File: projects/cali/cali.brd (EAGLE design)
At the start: 89.8 x 61.9 mm, 28 parts, among them T1 IRLML2502, T2 IRLML2502, T3 2N7002E, T4 IRLML2502

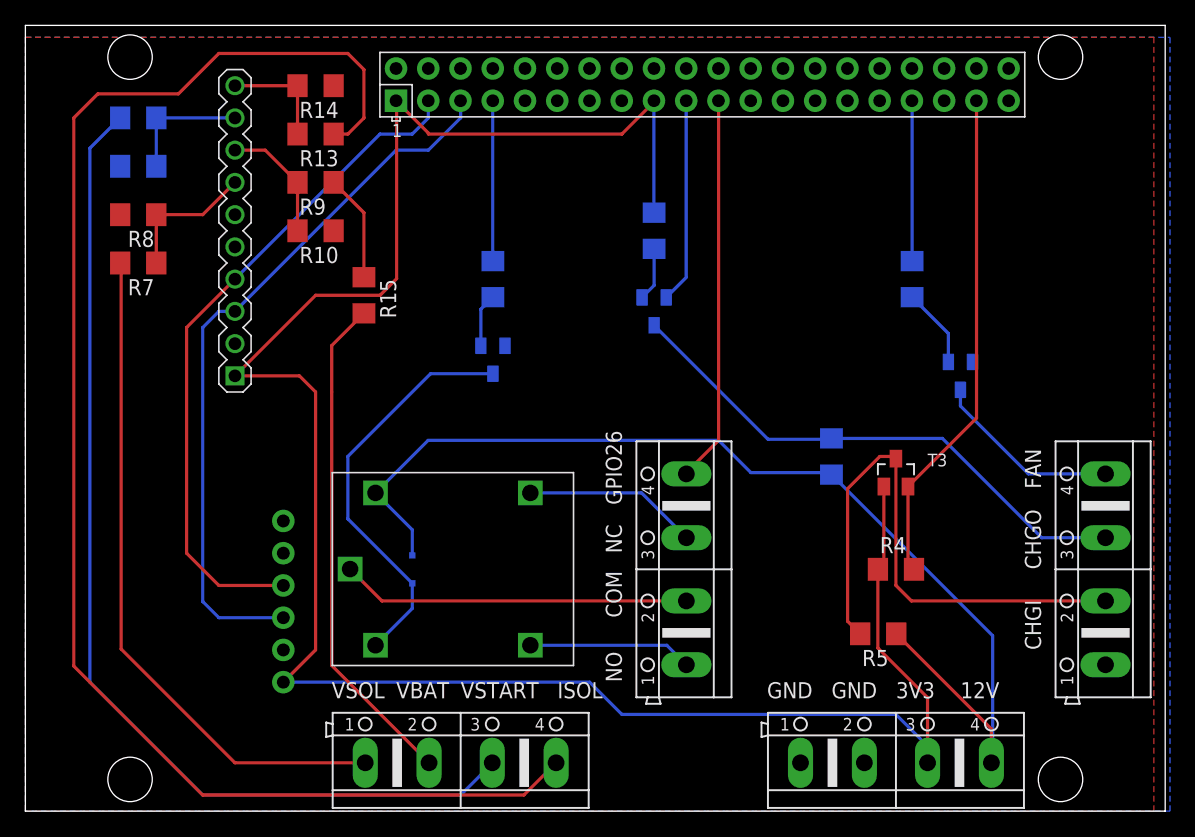
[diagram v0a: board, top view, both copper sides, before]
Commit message: Caliboard 1.2
- Fan output now has a PP stage
- Temp-sensor 4k7 pull up
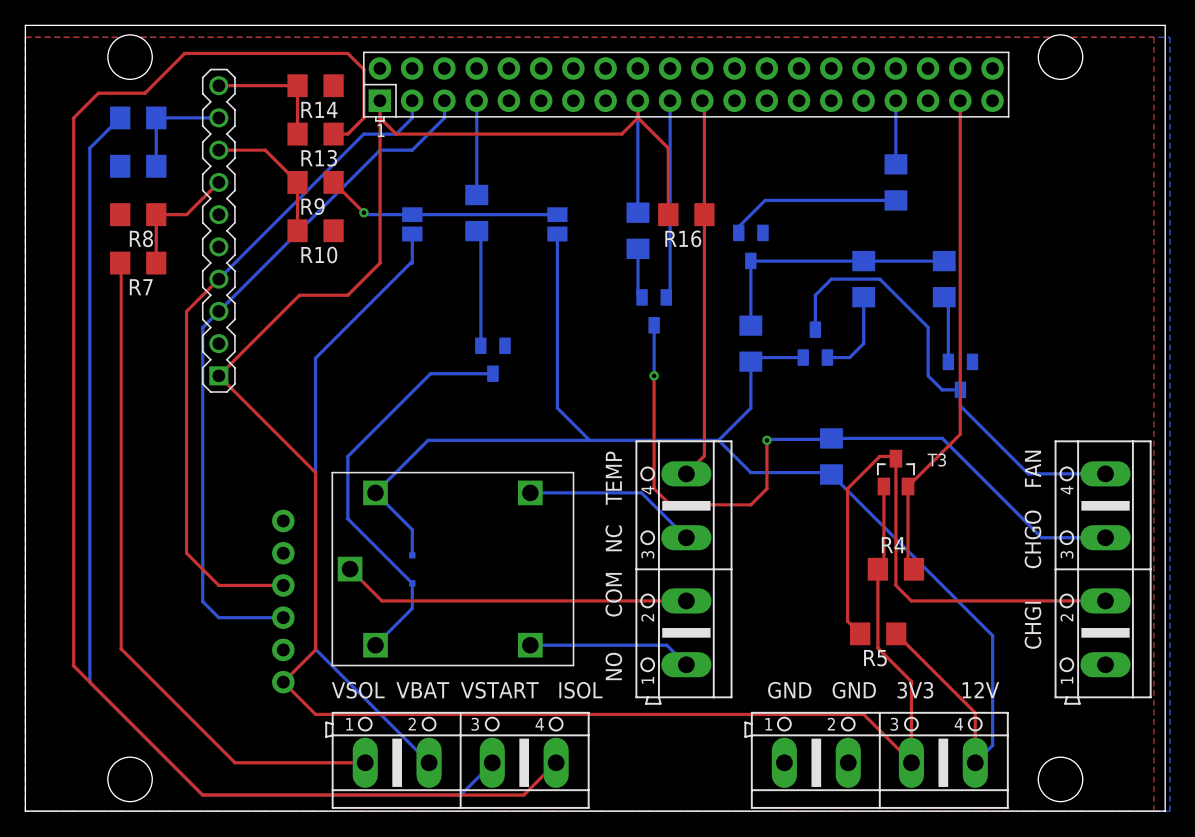
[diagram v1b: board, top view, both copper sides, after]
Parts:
- added R16: 4k7, rcl:R1206
- added R17: 10k, rcl:R1206
- added R18: 100, rcl:R1206
- added SJ1, SJ2: (no value), jumper:SJ
- added T5: IRLML6402, we-transistor:SOT23
- added T6: IRLML2502, we-transistor:SOT23
- R15: value 0 -> 100
- moved R15 39.4 mm to (66.0, 41.9), flipped to the bottom
- moved R6 5.36 mm to (35.6, 47.1)
- moved R1 2.54 mm to (72.4, 41.9)
- moved R2 1.27 mm to (48.3, 45.7)
- moved U$1 1.27 mm to (8.89, 45.7)
- moved U$2 1.27 mm to (19.6, 30.7)
- moved X2 1.27 mm to (67.3, 3.81)
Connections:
- removed net N$9: R15.2, X3.2
- new net /GPIO13: R1.1, R15.1, R17.1, T6.3
- new net N$12: R18.2, T6.1
- new net N$8: R15.2, T5.1
- new net V_BAT: SJ1.1, X3.2
- net +12V: now also R17.2, SJ2.2, T5.2
- net +3V3: now also R16.2
- net GND: now also T6.2
- net GPIO13: now also R18.1; no longer R1.1
- net GPIO9: now also R16.1
- net N$13: now also SJ1.2, SJ2.1; no longer R15.1
- net N$2: now also T5.3
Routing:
- net V_BAT: track 0.00 -> 48.6 mm
- net N$9: track 39.6 -> 0.00 mm
- net +12V: track 86.1 -> 115.0 mm
- net N$2: track 14.9 -> 35.4 mm
- net /GPIO13: track 0.00 -> 20.3 mm
- net N$11: track 42.6 -> 56.8 mm, vias 0 -> 2
- net N$12: track 0.00 -> 13.7 mm
- net N$13: track 8.46 -> 18.8 mm, vias 0 -> 1
- net GPIO13: track 12.6 -> 5.02 mm
- net N$8: track 0.00 -> 6.97 mm
- net GPIO4: track 12.6 -> 7.45 mm
- net N$4: track 4.22 -> 9.17 mm
- net +3V3: track 169.8 -> 172.9 mm
- net SCL: track 57.0 -> 55.7 mm
- net ADC3: track 8.74 -> 10.0 mm
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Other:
- board text added: "(c) Christian Eisendle"
- board text added: "Caliboard 1.2"
- board text added: "TEMP"
- board text removed: "Caliboard 1.1 (c) Christian Eisendle"
- board text removed: "GPIO26"

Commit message: Caliboard 1.4
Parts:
- removed D1: BAS316, nxp_60:SOD323(F)
- removed R15, R18, R2, R6: 100, rcl:R1206
- removed R17, R3, R5: 10k, rcl:R1206
- removed T1, T2, T4, T6: IRLML2502, we-transistor:SOT23
- removed T3: 2N7002E, nxp_60:SOT23
- removed T5: IRLML6402, we-transistor:SOT23
- added D2: BZX384-3V3, nxp_60:SOD323(F)
- added IC1: L293DD, st-microelectronics:SO20
- R1: value 100 -> DNP
- R4: value 1k -> 10k
- moved SJ2 27.6 mm to (37.0, 19.1), turned to 180 degrees
- moved SJ1 27.2 mm to (31.0, 19.1), turned to 180 degrees
- moved R1 26.7 mm to (73.7, 15.2), flipped to the top
- moved R4 24.7 mm to (73.7, 43.2), turned to 270 degrees
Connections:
- removed net /GPIO13: R1.1, R15.1, R17.1, T6.3
- removed net CHGI: R5.1, T3.3, X1.2
- removed net GPIO4: R6.1, U$2.7
- removed net N$1: D1.2, T4.3, U$4.A2
- removed net N$10: R2.1, T2.1
- removed net N$11: R3.1, T2.3, X1.3
- removed net N$12: R18.2, T6.1
- removed net N$4: R6.2, T4.1
- removed net N$8: R15.2, T5.1
- new net DRVOUT3: IC1.13, U$4.A1
- new net GPIO5: IC1.9, U$2.29
- new net GPIO6: IC1.12, U$2.31
- new net N$9: R1.1, R4.2, X1.2
- net +12V: now also IC1.10, IC1.20; no longer D1.1, R17.2, R3.2, R5.2, T5.2, U$4.A1
- net +3V3: now also IC1.1, IC1.11; no longer R2.2, R4.1, T3.1
- net GND: now also D2.2, IC1.14, IC1.15, IC1.16, IC1.17, IC1.19, IC1.4, IC1.5, IC1.6, IC1.7, R1.2, U$4.A2; no longer T1.2, T4.2, T6.2
- net GPIO10: no longer T2.2
- net GPIO13: now also IC1.2; no longer R18.1
- net GPIO26: now also D2.1, R4.1; no longer R4.2, T3.2
- net N$2: now also IC1.3; no longer T1.3, T5.3
- net N$6: now also IC1.8, X1.3; no longer R1.2, T1.1
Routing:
- net N$11: track 56.8 -> 0.00 mm, vias 2 -> 0
- net DRVOUT3: track 0.00 -> 53.5 mm
- net CHGI: track 43.8 -> 0.00 mm
- net N$9: track 0.00 -> 36.6 mm
- net GPIO13: track 5.02 -> 39.8 mm, vias 0 -> 2
- net V_BAT: track 48.6 -> 15.9 mm
- net N$1: track 32.3 -> 0.00 mm
- net GPIO26: track 38.8 -> 11.7 mm
- net +12V: track 115.0 -> 139.6 mm
- net GPIO5: track 0.00 -> 22.4 mm, vias 0 -> 1
- net N$13: track 18.8 -> 39.9 mm
- net /GPIO13: track 20.3 -> 0.00 mm
- net N$2: track 35.4 -> 15.4 mm
- net N$6: track 5.23 -> 23.1 mm
- net GPIO10: track 15.6 -> 0.00 mm
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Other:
- board text added: "Caliboard 1.4"
- board text removed: "Caliboard 1.2"

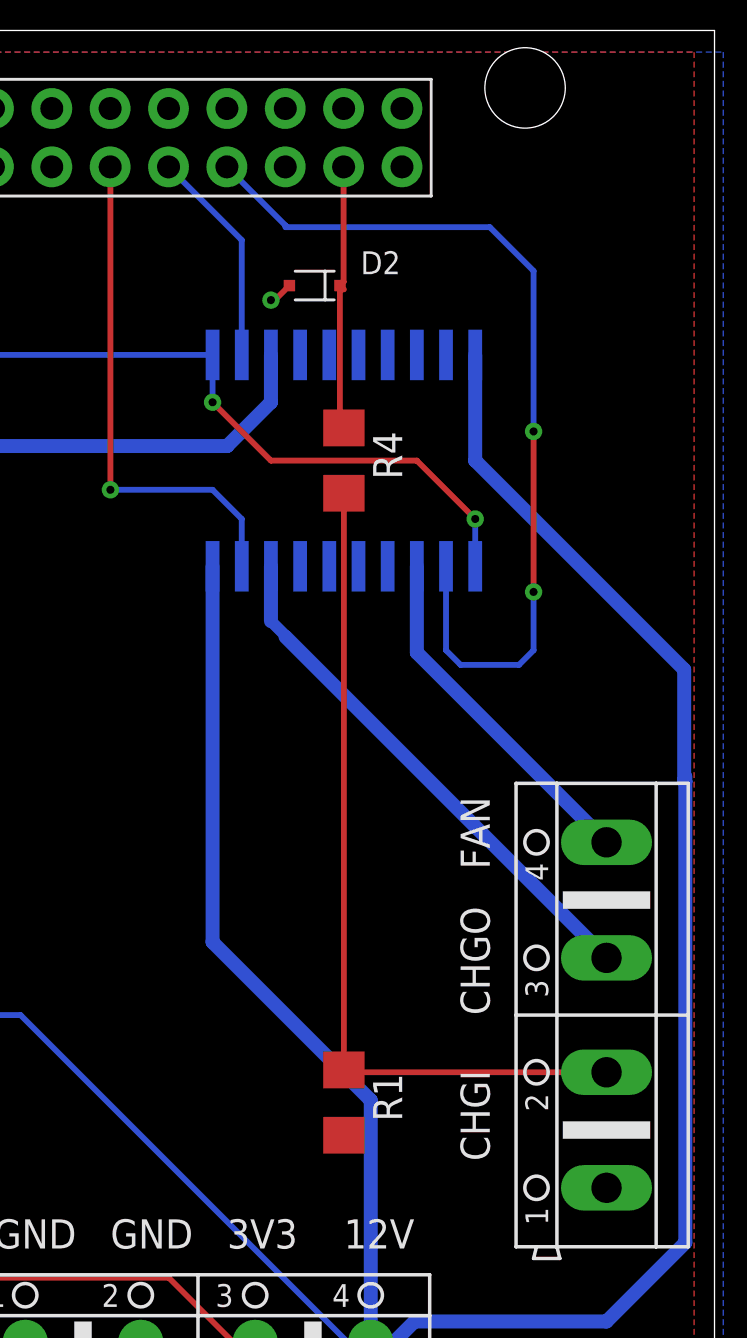
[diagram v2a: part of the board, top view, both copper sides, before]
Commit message: Add additional 12V input
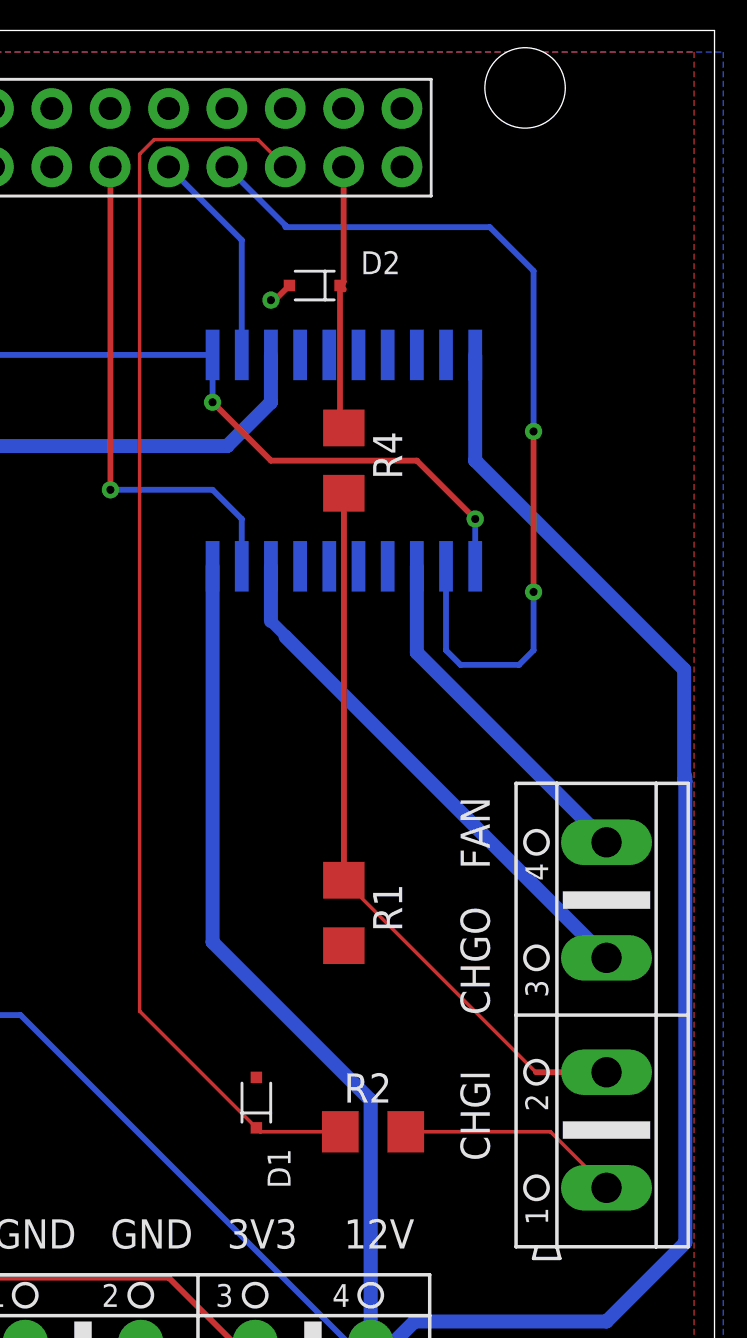
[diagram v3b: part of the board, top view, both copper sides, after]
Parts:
- added D1: BZX384-3V3, nxp_60:SOD323(F)
- added R2: 10k, rcl:R1206
- moved R1 8.26 mm to (73.7, 23.5)
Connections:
- new net N$1: R2.2, X1.1
- net GND: now also D1.2
- net GPIO19: now also D1.1, R2.1
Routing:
- net GPIO19: track 0.00 -> 55.3 mm
- net N$1: track 0.00 -> 9.75 mm
- net N$9: track 36.6 -> 31.7 mm
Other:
- board text added: "Caliboard 1.5"
- board text removed: "Caliboard 1.4"
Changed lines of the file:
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@@
 <?xml version="1.0" encoding="utf-8"?>
 <!DOCTYPE eagle SYSTEM "eagle.dtd">
-<eagle version="9.5.0">
+<eagle version="9.6.2">
 <drawing>
 <settings>
@@
 </layers>
 <board>
+<fusionsync huburn="a.YnVzaW5lc3M6ZWlzZW5kbGU" projecturn="a.YnVzaW5lc3M6ZWlzZW5kbGUjRDIwMjEwMjAxMzc4MTcyOTAx" f3durn="urn:adsk.wipprod:dm.lineage:eCGwQmRcSUigPiUjFh4LgA" pcbguid="cfd05f05-6c82-4ab4-a93a-90a34d57cd22" lastpulledtime="" lastsyncedchangeguid="" latestrevisionid="486f0e6d-648d-4e1b-b5ac-af7fca4b0c5f" lastsyncedrevisionid="486f0e6d-648d-4e1b-b5ac-af7fca4b0c5f" lastboardhashguid="fca3c6b0-a0bf-6b08-91ea-aeebe4905dde" lastpushedtime="2022-08-21T08:59:15Z" linktopcb3d="true"/>
 <plain>
 <wire x1="0" y1="0" x2="89.79" y2="0" width="0" layer="20"/>
@@
 <text x="46.99" y="10.16" size="1.27" layer="25" rot="R90">NO</text>
 <text x="46.99" y="24.13" size="1.27" layer="25" rot="R90">TEMP</text>
-<text x="10.16" y="33.02" size="1.778" layer="26" rot="MR270">Caliboard 1.4</text>
+<text x="10.16" y="33.02" size="1.778" layer="26" rot="MR270">Caliboard 1.5</text>
 <text x="6.35" y="41.91" size="1.778" layer="26" rot="MR270">(c) Christian Eisendle</text>
 </plain>
@@
 <attribute name="NAME" x="74.39" y="51.29" size="1" layer="25" font="vector"/>
 </element>
-<element name="R1" library="rcl" package="R1206" value="DNP" x="73.66" y="15.24" smashed="yes" rot="R270">
-<attribute name="NAME" x="74.93" y="16.51" size="1.27" layer="25" rot="R270"/>
-<attribute name="POPULARITY" value="41" x="73.66" y="15.24" size="1.778" layer="27" rot="R270" display="off"/>
-<attribute name="SPICEPREFIX" value="R" x="73.66" y="15.24" size="1.778" layer="27" rot="R270" display="off"/>
+<element name="R1" library="rcl" package="R1206" value="DNP" x="73.66" y="23.495" smashed="yes" rot="R270">
+<attribute name="NAME" x="74.93" y="24.765" size="1.27" layer="25" rot="R270"/>
+<attribute name="POPULARITY" value="41" x="73.66" y="23.495" size="1.778" layer="27" rot="R270" display="off"/>
+<attribute name="SPICEPREFIX" value="R" x="73.66" y="23.495" size="1.778" layer="27" rot="R270" display="off"/>
+</element>
+<element name="R2" library="rcl" package="R1206" value="10k" x="74.93" y="13.97" smashed="yes">
+<attribute name="NAME" x="73.66" y="15.24" size="1.27" layer="25"/>
+<attribute name="POPULARITY" value="41" x="74.93" y="13.97" size="1.778" layer="27" display="off"/>
+<attribute name="SPICEPREFIX" value="R" x="74.93" y="13.97" size="1.778" layer="27" display="off"/>
+<attribute name="VALUE" x="73.66" y="11.43" size="1.27" layer="27"/>
+</element>
+<element name="D1" library="nxp_60" package="SOD323(F)" value="BZX384-3V3" x="69.85" y="15.24" smashed="yes" rot="R270">
+<attribute name="NAME" x="70.34" y="13.24" size="1" layer="25" font="vector" rot="R270"/>
+<attribute name="VALUE" x="68.85" y="13.24" size="1" layer="27" font="vector" rot="R270"/>
 </element>
 </elements>
@@
 <wire x1="70.655" y1="50.165" x2="70.485" y2="50.165" width="0.254" layer="1"/>
 <via x="70.485" y="50.165" extent="1-16" drill="0.35"/>
+<contactref element="D1" pad="2"/>
 </signal>
 <signal name="+3V3">
@@
 <signal name="GPIO19">
 <contactref element="U$2" pad="35"/>
+<contactref element="R2" pad="1"/>
+<contactref element="D1" pad="1"/>
+<wire x1="73.508" y1="13.97" x2="70.02" y2="13.97" width="0.1524" layer="1"/>
+<wire x1="70.02" y1="13.97" x2="69.935" y2="14.055" width="0.1524" layer="1"/>
+<wire x1="69.935" y1="14.055" x2="69.85" y2="14.14" width="0.1524" layer="1"/>
+<wire x1="71.108" y1="55.964" x2="69.922" y2="57.15" width="0.1524" layer="1"/>
+<wire x1="65.405" y1="57.15" x2="64.77" y2="56.515" width="0.1524" layer="1"/>
+<wire x1="64.77" y1="19.22" x2="69.85" y2="14.14" width="0.1524" layer="1"/>
+<wire x1="69.922" y1="57.15" x2="65.405" y2="57.15" width="0.1524" layer="1"/>
+<wire x1="64.77" y1="56.515" x2="64.77" y2="19.22" width="0.1524" layer="1"/>
 </signal>
 <signal name="ADC0">
@@
 <contactref element="R4" pad="2"/>
 <contactref element="R1" pad="1"/>
-<wire x1="85.09" y1="16.5608" x2="73.7612" y2="16.5608" width="0.254" layer="1"/>
-<wire x1="73.7612" y1="16.5608" x2="73.66" y2="16.662" width="0.1524" layer="1"/>
-<wire x1="73.66" y1="16.662" x2="73.66" y2="41.758" width="0.254" layer="1"/>
+<wire x1="85.09" y1="16.5608" x2="82.0162" y2="16.5608" width="0.254" layer="1"/>
+<wire x1="82.0162" y1="16.5608" x2="73.66" y2="24.917" width="0.1524" layer="1"/>
+<wire x1="73.66" y1="24.917" x2="73.66" y2="41.758" width="0.254" layer="1"/>
 </signal>
 <signal name="DRVOUT3">
@@
 <wire x1="63.5" y1="41.91" x2="63.5" y2="55.952" width="0.254" layer="1"/>
 <wire x1="63.5" y1="55.952" x2="63.488" y2="55.964" width="0.254" layer="1"/>
+</signal>
+<signal name="N$1">
+<contactref element="X1" pad="1"/>
+<contactref element="R2" pad="2"/>
+<wire x1="76.352" y1="13.97" x2="82.6516" y2="13.97" width="0.1524" layer="1"/>
+<wire x1="82.6516" y1="13.97" x2="85.09" y2="11.5316" width="0.1524" layer="1"/>
 </signal>
 </signals>
@@
 </note>
 <note version="8.3" severity="warning">
+Since Version 8.3, EAGLE supports Fusion synchronisation.
+This feature will not be available in this version and saving
+the document will break the link to the Fusion PCB feature.
+</note>
+<note version="8.3" severity="warning">
